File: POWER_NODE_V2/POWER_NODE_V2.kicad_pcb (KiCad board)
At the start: 2 copper layers, 178 x 144 mm, 126 parts, among them J1 TE_3-641119-2, J10 CONN_02X07, J11 CONN_01X04, J12 CONN_01X04, J13 TE_3-641119-2, J14 TE_3-641119-2, J15 TE_3-641119-2, J16 3-641215-3, J17 3-641215-3, J18 3-641215-3, J19 3-641215-3, J2 TE_3-641119-2, J20 3-641215-3, J21 3-641215-3, J3 Keystone_3544-2, J4 Keystone_3544-2, J5 5-146130-9, J6 I2C2_J10_8_9, J7 5-146130-9, J8 CONN_01X01, J9 TE_3-641119-2, Q1 BSS84, Q2 BSS84, Q3 BSS84, Q4 BSS84, Q5 BSS84, Q6 BSS84, Q7 BSS84, U1 LM1117MP-3.3/NOPB, U10 DS2482S-100+T&R, U11 DS2482S-100+T&R, U12 NCV8405ADTRKG, U13 MAX14850AEE+, U14 MAX14850AEE+, U15 TL783CKTTR, U16 TL783CKTTR, U17 AMC1100DWV, U18 AMC1100DWV, U19 NUD3124LT1G, U2 R-745.0P, U20 RTE24024, U3 DS2482S-100+T&R, U4 DS2482S-100+T&R, U5 DS2482S-100+T&R, U6 TSYS01, U7 MS5607-02BA03, U8 DS2482S-100+T&R, U9 DS2482S-100+T&R

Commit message: All modelled, schematics and mechanical just need a double check
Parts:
- removed the BMS_Outline at (176.0, 92.0)
- added BMS_Outline: BMS_Outline, rLoop_Footprints:BMS_Outline, F.Cu at (176.0, 92.0)
- D6, D9: footprint Diodes_THT:D_DO-201_P15.24mm_Horizontal -> rLoop_Footprints:D_DO-201_P15.24mm_Horizontal
- F1: footprint rLoop Footprints:2920L300_15DR -> rLoop_Footprints:2920L300_15DR
- J10: value CONN_02X07 -> 5-534998-7
- J6: footprint Pin_Headers:Pin_Header_Straight_1x02_Pitch2.54mm_SMD_Pin1Left -> Pin_Headers:Pin_Header_Straight_1x02_Pitch2.54mm
- J8: value CONN_01X01 -> 3-641215-3; footprint Pin_Headers:Pin_Header_Straight_1x01_Pitch2.54mm -> rLoop_Footprints:3-641215-3_3Pin_Latching_Header
- U15, U16: footprint TO_SOT_Packages_SMD:TO-263-3_TabPin4 -> rLoop_Footprints:tl783ckttr
- moved C21 29.7 mm to (132.2, 117.6), turned to 90 degrees
- moved U14 28.1 mm to (134.8, 122.2)
- moved C22 11.4 mm to (132.2, 127.4)
- moved U13 10.8 mm to (134.8, 132.0)
- moved R11 10.7 mm to (129.2, 134.2)
- moved R12 10.3 mm to (136.8, 128.0), turned to 180 degrees
- moved J15 6.77 mm to (33.2, 65.0)
- moved D6 4.14 mm to (62.0, 30.8)
- moved R32 4.07 mm to (32.0, 75.5)
- moved D8 3.78 mm to (32.2, 73.5)
- moved J10 2.99 mm to (149.0, 134.8), turned to 180 degrees
- moved R4 1.50 mm to (42.5, 123.5)
- moved D5 1.50 mm to (53.2, 127.0)
- moved J6 1.27 mm to (125.0, 145.5)
- moved J9 0.96 mm to (102.2, 28.5)
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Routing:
- net BATT_N_HOT: track 115.8 -> 74.3 mm
- net /BMS Interface/BMS_ALERT: track 92.1 -> 120.1 mm
- net /BMS Interface/BMS_FAULT: track 87.8 -> 115.4 mm
- net /BMS Interface/BMS_CONV: track 85.7 -> 112.9 mm
- net /BMS Interface/1-Wire: track 76.8 -> 101.6 mm
- net /BMS Interface/BMS_MOSI: track 108.3 -> 122.5 mm
- net /BMS Interface/BMS_DRDY: track 95.6 -> 109.8 mm
- net /BMS Interface/BMS_MISO: track 109.2 -> 122.8 mm
- net /BMS Interface/BMS_NCS: track 100.4 -> 113.6 mm
- net Net-(D4-Pad2): track 17.8 -> 6.98 mm
- net Net-(D3-Pad2): track 17.8 -> 7.30 mm
- net /BMS Interface/BMS_COMMS_EN: track 42.5 -> 51.6 mm, vias 0 -> 1
- net +3V3: track 534.8 -> 526.9 mm, vias 13 -> 16
- net Net-(J10-Pad2): track 30.5 -> 22.9 mm, vias 1 -> 2
- net Net-(J10-Pad8): track 18.3 -> 10.9 mm
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- added copper zone on F.Cu, net Net-(D3-Pad2)
- added copper zone on F.Cu, net Net-(D4-Pad2)
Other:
- board text added: "+"
- board text added: "-"
- board text added: "- +"
- board text added: "1"
- board text added: "1 Wre"
- board text added: "1-W"
- board text added: "10"
- board text added: "10A MINI-AUTO"
- board text added: "11"
- board text added: "13"
- board text added: "2"
- board text added: "20"
- board text added: "21"
- board text added: "24V"
- board text added: "3.3"
- board text added: "3.3V"
- board text added: "30"
- board text added: "31"
- board text added: "40"
- board text added: "5V"
- board text added: "ALERT"
- board text added: "BATT I"
- board text added: "BATTERY TEMP 1-WIRE BUS X6"
- board text added: "BMS 5V"
- board text added: "BMS FAN"
- board text added: "BMS GND"
- board text added: "Batt V"
- board text added: "CHG I"
- board text added: "CHG RLY"
- board text added: "CHG V"
- board text added: "COMMS_EN"
- board text added: "CONV"
- board text added: "DRDY"
- board text added: "FAULT"
- board text added: "GND"
- board text added: "I"
- board text added: "MISO"
- board text added: "MOSI"
- board text added: "N 3V3"
- board text added: "N GND"
- board text added: "NCS"
- board text added: "Ref"
- board text added: "SCK"
- board text added: "WDT"

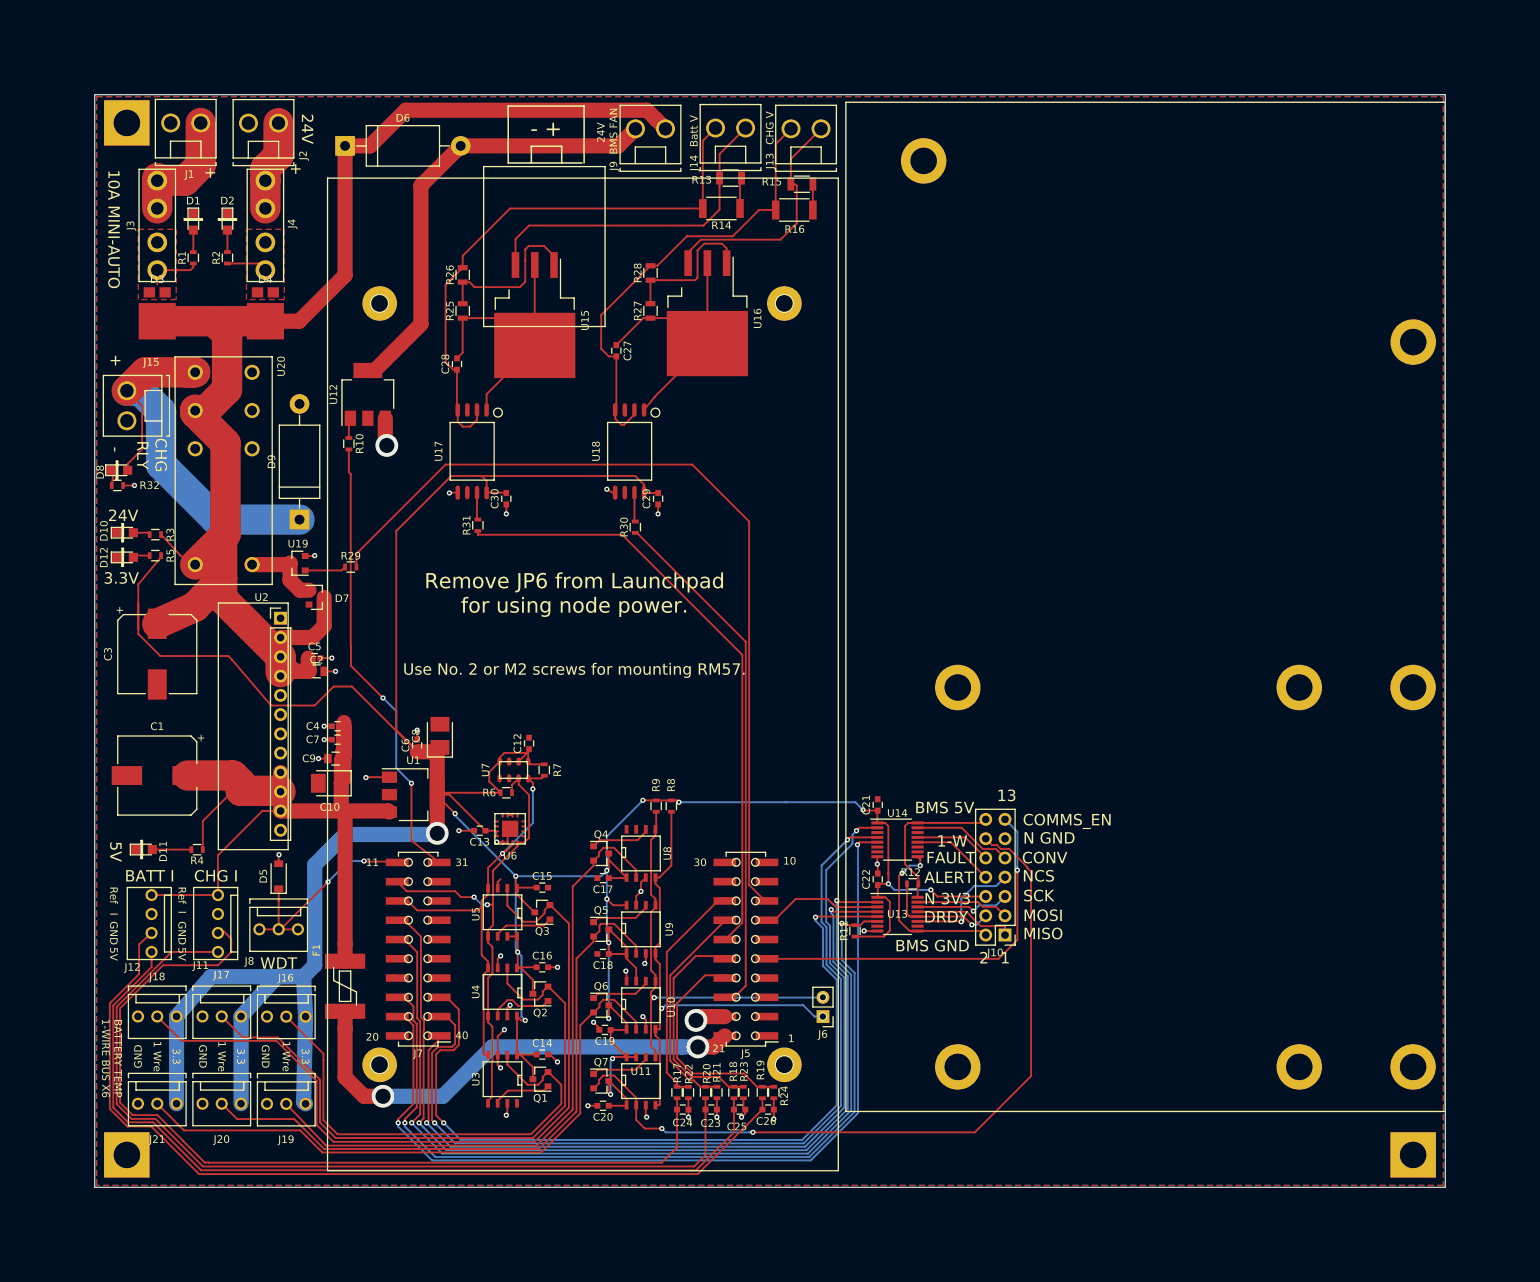
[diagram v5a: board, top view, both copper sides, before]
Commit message: Added tooling holes & fiducial marks
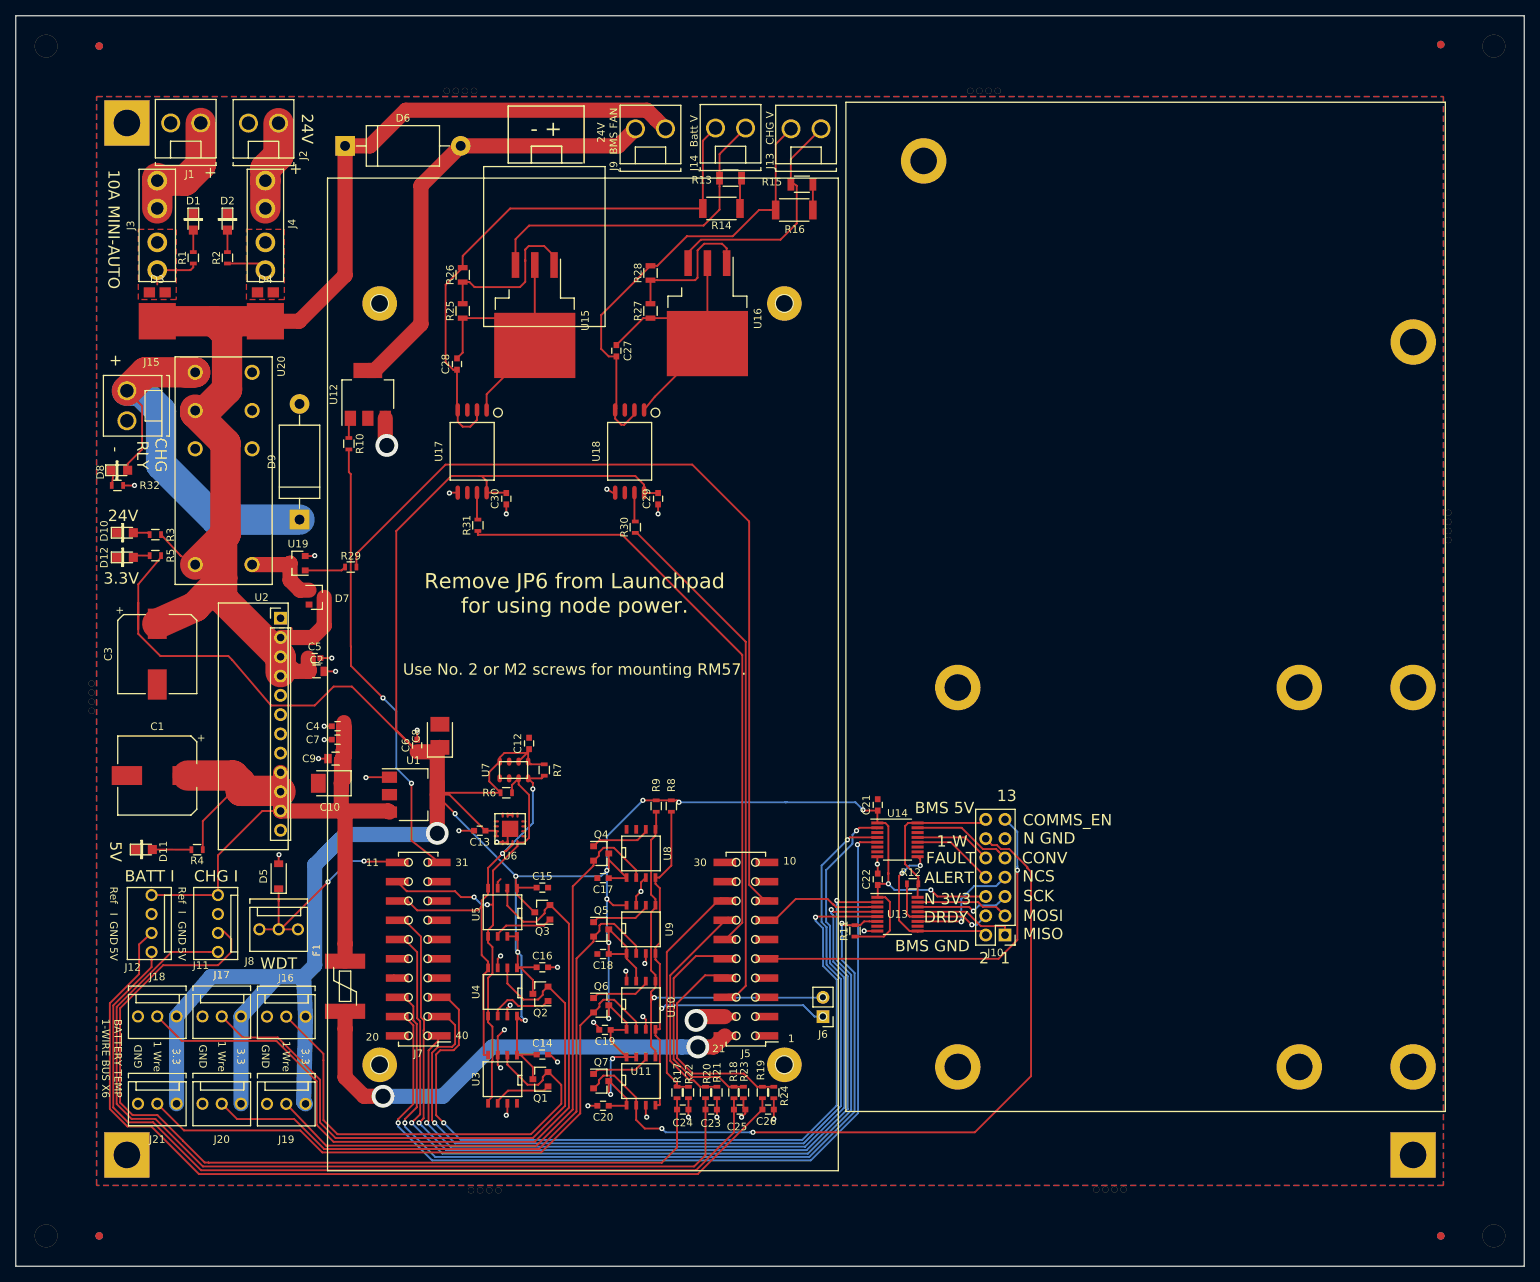
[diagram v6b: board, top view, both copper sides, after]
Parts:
- added REF**: Fiducial_1mm, rLoop_Footprints:Fiducial_1mm, F.Cu at (206.4, 174.4)
- added REF**: tooling_3mm, rLoop_Footprints:tooling_3mm, F.Cu at (22.6, 174.4)
- added REF**: mouse_bite, rLoop_Footprints:mouse_bite, F.Cu at (28.6, 103.4)
- added REF**: mouse_bite, rLoop_Footprints:mouse_bite, F.Cu at (162.8, 168.3)
- added REF**: mouse_bite, rLoop_Footprints:mouse_bite, F.Cu at (146.2, 23.5)
- added REF**: mouse_bite, rLoop_Footprints:mouse_bite, F.Cu at (207.4, 80.9)
- added REF**: Fiducial_1mm, rLoop_Footprints:Fiducial_1mm, B.Cu at (29.6, 17.6)
- added REF**: Fiducial_1mm, rLoop_Footprints:Fiducial_1mm, B.Cu at (206.4, 17.4)
- added REF**: Fiducial_1mm, rLoop_Footprints:Fiducial_1mm, B.Cu at (206.4, 174.4)
- added REF**: Fiducial_1mm, rLoop_Footprints:Fiducial_1mm, B.Cu at (29.6, 174.4)
- added REF**: Fiducial_1mm, rLoop_Footprints:Fiducial_1mm, F.Cu at (29.6, 174.4)
- added REF**: Fiducial_1mm, rLoop_Footprints:Fiducial_1mm, F.Cu at (29.6, 17.6)
- added REF**: Fiducial_1mm, rLoop_Footprints:Fiducial_1mm, F.Cu at (206.4, 17.4)
- added REF**: mouse_bite, rLoop_Footprints:mouse_bite, F.Cu at (77.2, 23.5)
- added REF**: mouse_bite, rLoop_Footprints:mouse_bite, F.Cu at (80.4, 168.4)
- added REF**: tooling_3mm, rLoop_Footprints:tooling_3mm, F.Cu at (22.6, 17.6)
- added REF**: tooling_3mm, rLoop_Footprints:tooling_3mm, F.Cu at (213.4, 17.6)
- added REF**: tooling_3mm, rLoop_Footprints:tooling_3mm, F.Cu at (213.4, 174.4)
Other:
- board size 178 x 144 mm -> 198.8 x 164.8 mm

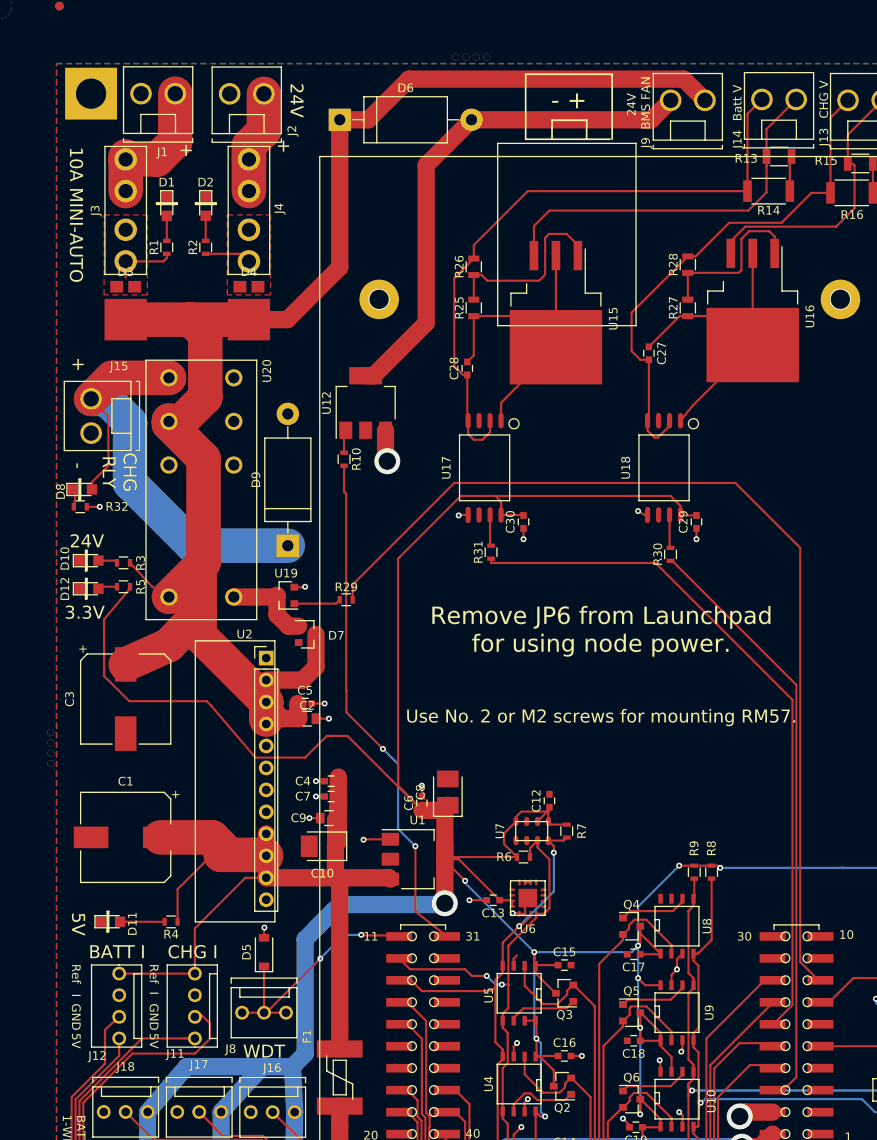
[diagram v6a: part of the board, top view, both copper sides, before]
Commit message: added cooling solenoid to pcb
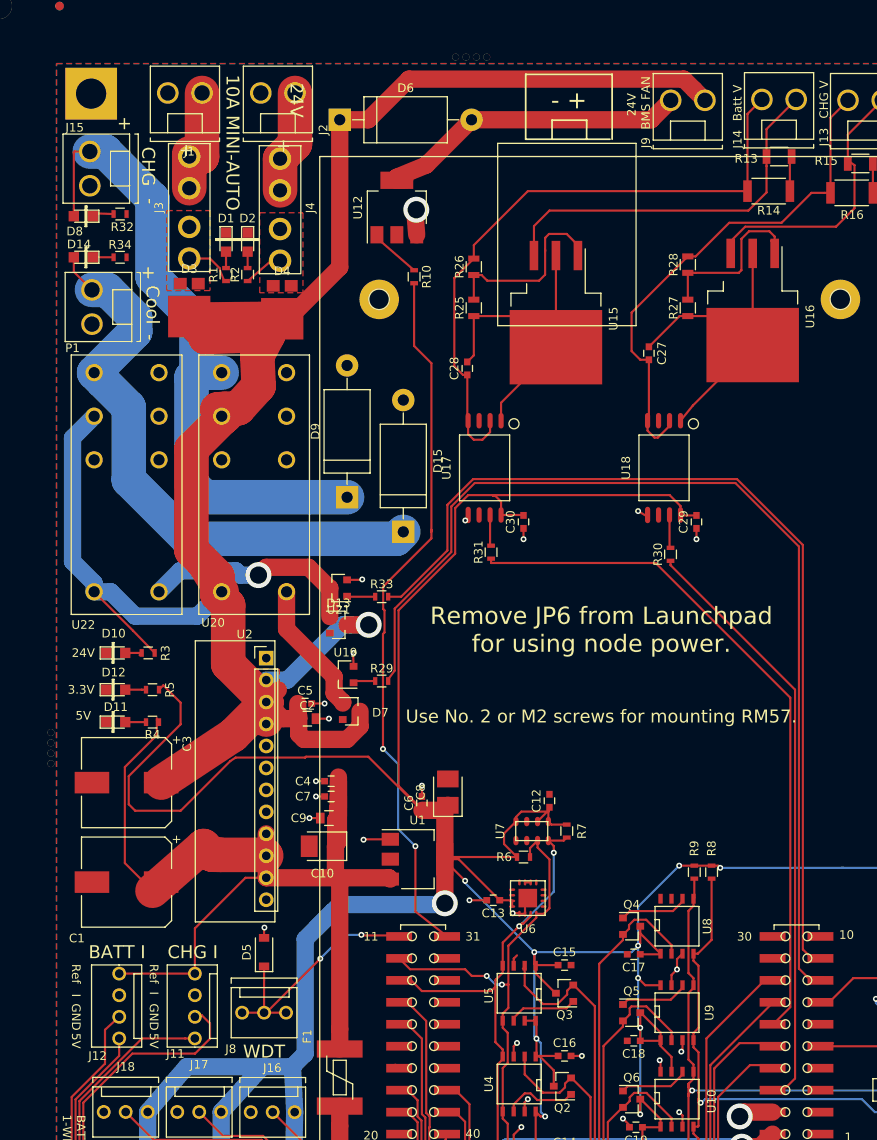
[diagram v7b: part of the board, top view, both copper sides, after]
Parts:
- added D13: BAS16, Diodes_SMD:D_SOT-23_ANK, F.Cu at (61.9, 89.2)
- added D14: EL-17-21VGC/TR8, rLoop_Footprints:LED_0805, F.Cu at (32.4, 46.6)
- added D15: 1N4004, rLoop_Footprints:1N4004, F.Cu at (69.3, 78.4)
- added P1: TE_3-641119-2, rLoop_Footprints:3-641119-2_TE_2P_MTA156_HDR, F.Cu at (33.4, 52.4)
- added R33: 50 / .1 W / 10% / SMD 0603, Resistors_SMD:R_0603, F.Cu at (66.8, 85.9)
- added R34: 4.7k / .1W / 10% / SMD 0603, Resistors_SMD:R_0603, F.Cu at (36.6, 46.6)
- added U21: NUD3124LT1G, TO_SOT_Packages_SMD:SOT-23, F.Cu at (61.9, 84.9)
- added U22: RTE24024, rLoop_Footprints:RTE24024, F.Cu at (37.4, 80.2)
- J6: value I2C2_J10_8_9 -> 826926-2
- moved R32 34.2 mm to (36.6, 41.6)
- moved D8 31.6 mm to (32.4, 41.9), turned to 180 degrees
- moved J15 28.6 mm to (33.1, 36.4)
- moved R4 23.2 mm to (40.4, 100.4)
- moved D11 23.1 mm to (36.1, 100.4)
- moved U12 22.9 mm to (68.6, 40.9)
- moved R10 22.6 mm to (70.6, 48.9)
- moved R5 12.4 mm to (40.4, 96.7)
- moved D12 12.1 mm to (36.1, 96.7)
- moved U19 11.4 mm to (62.6, 94.9)
- moved D10 11.1 mm to (36.1, 92.4)
- moved R3 10.8 mm to (39.9, 92.4)
- moved D7 10.3 mm to (63.4, 99.2)
- moved R29 10.3 mm to (66.8, 95.7)
- moved C3 9.67 mm to (37.4, 107.4), turned to 180 degrees
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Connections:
- J5 pad 9: Net-(J5-Pad9) -> /Cooling_Solenoid/COOLING_SOLENOID
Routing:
- net /Cooling_Solenoid/COOLING_SOLENOID: track 0.00 -> 109.1 mm
- net +24V: track 183.0 -> 253.3 mm, vias 0 -> 1
- net Net-(D14-Pad2): track 0.00 -> 68.3 mm
- net Net-(D13-Pad2): track 0.00 -> 25.6 mm, vias 0 -> 1
- net Net-(D6-Pad2): track 59.2 -> 36.3 mm
- net /BMS Interface/BMS_FAN: track 59.4 -> 82.2 mm
- net Net-(D8-Pad2): track 57.4 -> 76.6 mm
- net +5V: track 110.9 -> 124.5 mm
- net /RM57 Core/CHG_RLY: track 112.9 -> 119.7 mm
- net Net-(D7-Pad2): track 10.6 -> 15.8 mm
- net Net-(R10-Pad1): track 2.68 -> 6.24 mm
- net +3V3: track 526.9 -> 523.4 mm
- net Net-(R33-Pad1): track 0.00 -> 3.27 mm
- net Net-(J1-Pad2): track 16.1 -> 12.9 mm
- net Net-(R29-Pad1): track 5.44 -> 2.58 mm
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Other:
- board text added: "CHG"
- board text added: "Cool"
- board text removed: "CHG RLY"
